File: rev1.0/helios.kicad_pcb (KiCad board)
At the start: 4 copper layers, 17.8 x 33 mm, 61 parts, among them J1 USB_C_Receptacle_USB2.0, J2 helios-pinout, Q1 2N7002VC-, Q2 2N7002VC-, SW1 SWITCH, U1 USBLC6-2P6, U2 TLV75533PDQNR, U3 W25Q128JVPIQ, U4 RP2040, U5 74LVC1T45, Y1 12MHz

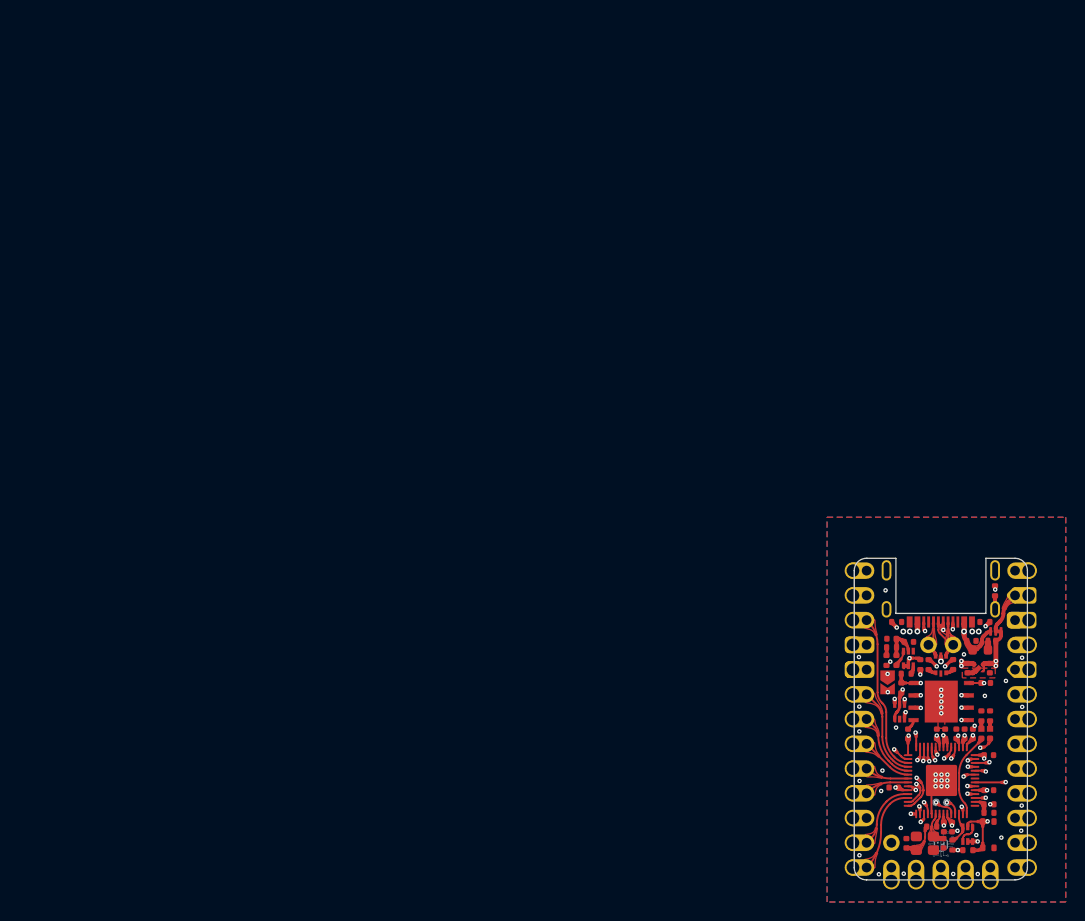
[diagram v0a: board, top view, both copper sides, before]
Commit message: widen tabs
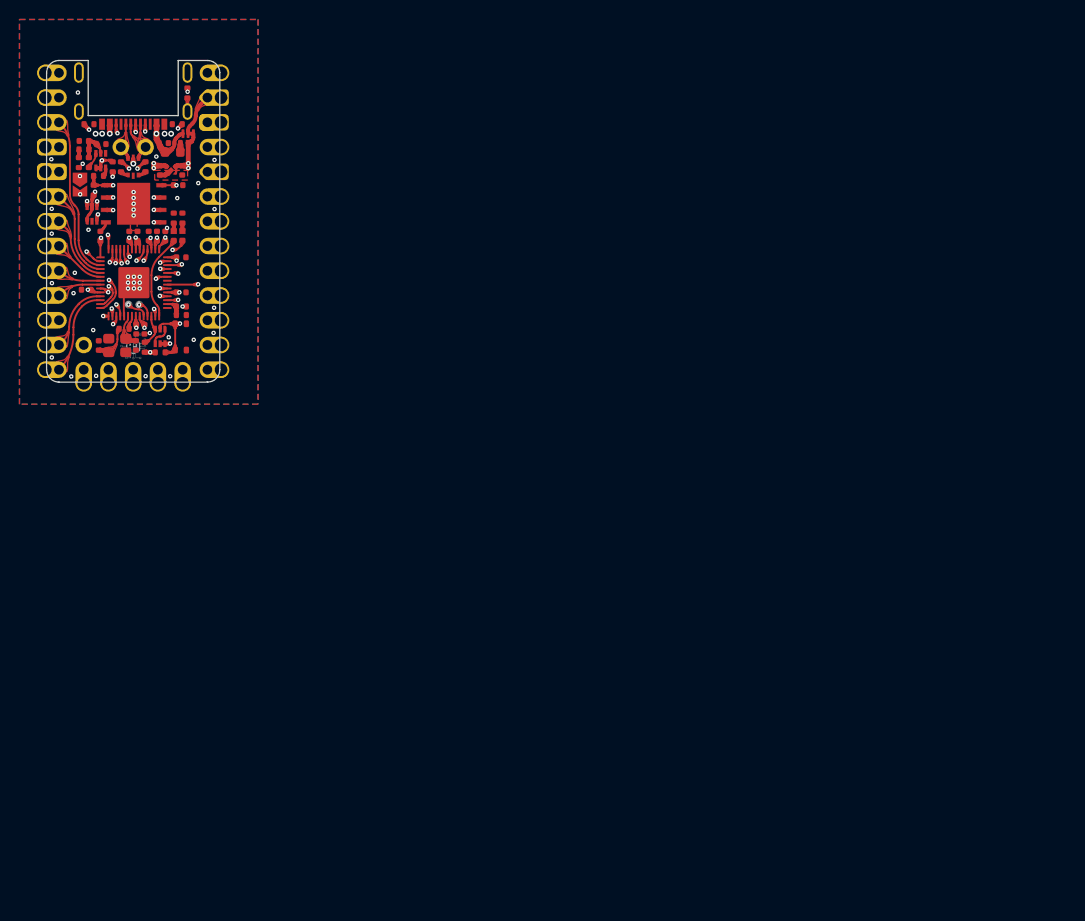
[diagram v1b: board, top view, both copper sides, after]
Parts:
- moved REF** 97.7 mm to (69.5, 81.2)
- moved R9 97.4 mm to (72.4, 93.6)
- moved SW1 97.4 mm to (80.8, 110.2)
- moved U1 97.4 mm to (75.9, 92.7)
- moved C1 97.4 mm to (70.9, 90.0)
- moved C12 97.4 mm to (80.9, 105.6)
- moved C14 97.4 mm to (76.4, 99.8)
- moved C15 97.4 mm to (71.1, 105.3)
- moved C16 97.4 mm to (72.6, 99.8)
- moved C3 97.4 mm to (79.1, 90.3)
- moved C9 97.4 mm to (78.4, 99.8)
- moved D2 97.4 mm to (80.1, 99.8)
- moved JP2 97.4 mm to (81.6, 89.3)
- moved Q2 97.4 mm to (72.6, 92.1)
- moved R1 97.4 mm to (78.7, 111.8)
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
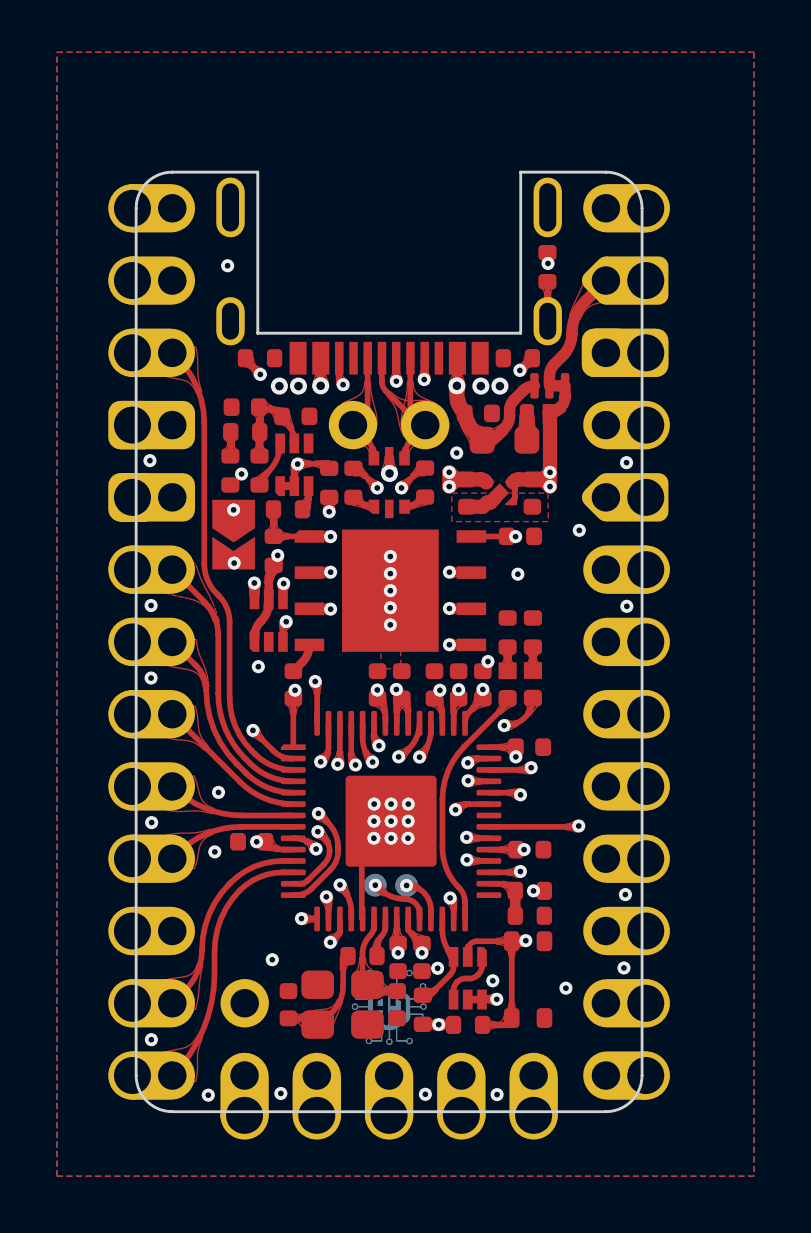
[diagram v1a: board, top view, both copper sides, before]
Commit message: widen tabs even more
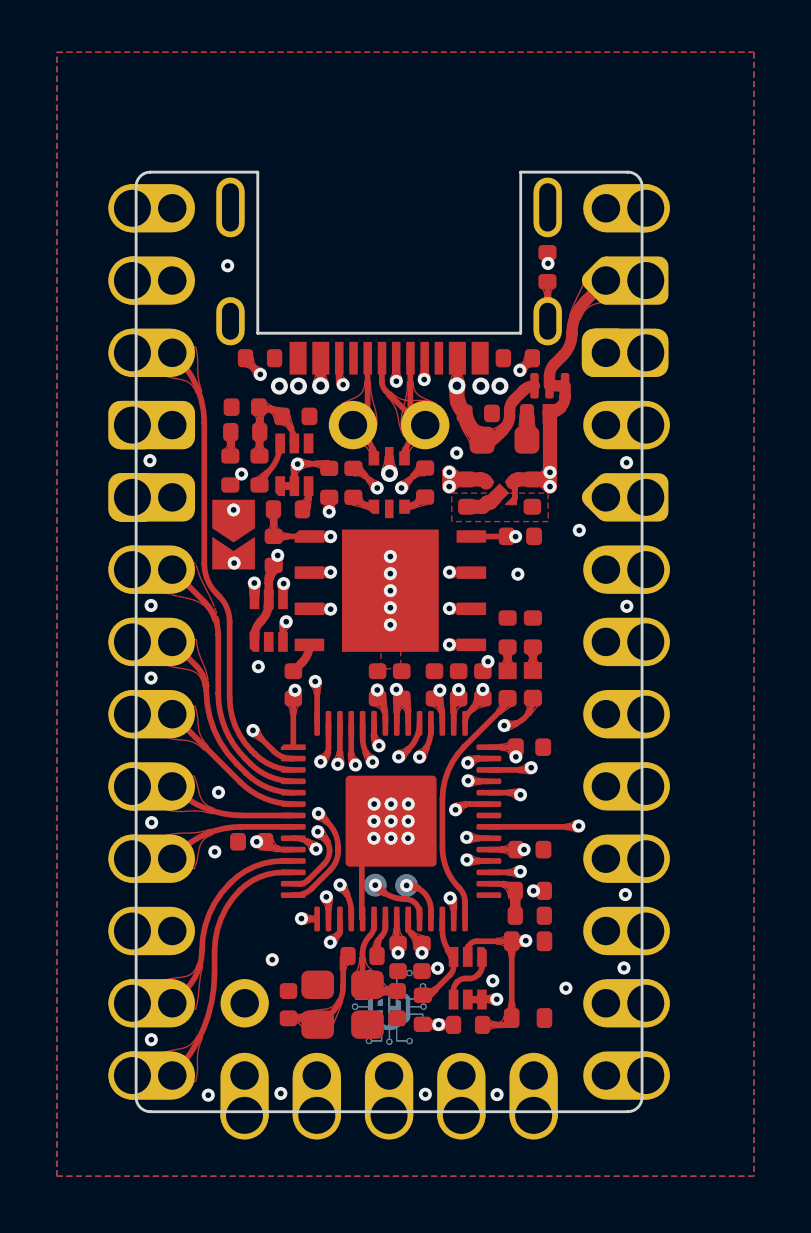
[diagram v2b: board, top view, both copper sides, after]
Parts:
- removed the REF** at (82.8, 115.2)
- removed the REF** at (69.1, 115.2)
- added REF**: Tab, kikit:Tab, F.Cu at (83.3, 115.3)
- added REF**: Tab, kikit:Tab, F.Cu at (68.6, 115.3)
- moved REF** 0.30 mm to (82.6, 81.3)
- moved REF** 0.28 mm to (69.3, 81.3)
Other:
- outline, holes or cut-outs redrawn
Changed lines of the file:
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@@
         (effects (font (size 0.8 0.8) (thickness 0.12)) (justify mirror))
     )
-    (fp_line (start -8.89 -16.51) (end -8.89 13.97)
+    (fp_line (start -8.89 -17.28) (end -8.89 14.74)
       (stroke (width 0.1) (type solid)) (layer "Edge.Cuts"))
-    (fp_line (start -7.62 15.24) (end 7.62 15.24)
+    (fp_line (start -8.39 15.24) (end 8.39 15.24)
       (stroke (width 0.1) (type solid)) (layer "Edge.Cuts"))
-    (fp_line (start 8.89 13.97) (end 8.89 -16.51)
-      (stroke (width 0.1) (type solid)) (layer "Edge.Cuts"))
-    (fp_arc (start -8.89 -16.51) (mid -8.518026 -17.408026) (end -7.62 -17.78)
-      (stroke (width 0.1) (type solid)) (layer "Edge.Cuts"))
-    (fp_arc (start -7.62 15.24) (mid -8.518026 14.868026) (end -8.89 13.97)
-      (stroke (width 0.1) (type solid)) (layer "Edge.Cuts"))
-    (fp_arc (start 7.62 -17.78) (mid 8.518026 -17.408026) (end 8.89 -16.51)
-      (stroke (width 0.1) (type solid)) (layer "Edge.Cuts"))
-    (fp_arc (start 8.89 13.97) (mid 8.518026 14.868026) (end 7.62 15.24)
+    (fp_line (start 8.89 14.74) (end 8.89 -17.28)
       (stroke (width 0.1) (type solid)) (layer "Edge.Cuts"))
+    (fp_arc (start -8.89 -17.28) (mid -8.743553 -17.633553) (end -8.39 -17.78)
+      (stroke (width 0.1) (type default)) (layer "Edge.Cuts"))
+    (fp_arc (start -8.39 15.24) (mid -8.743553 15.093553) (end -8.89 14.74)
+      (stroke (width 0.1) (type default)) (layer "Edge.Cuts"))
+    (fp_arc (start 8.39 -17.78) (mid 8.743553 -17.633553) (end 8.89 -17.28)
+      (stroke (width 0.1) (type default)) (layer "Edge.Cuts"))
+    (fp_arc (start 8.89 14.74) (mid 8.743553 15.093553) (end 8.39 15.24)
+      (stroke (width 0.1) (type default)) (layer "Edge.Cuts"))
     (pad "1" thru_hole circle (at -9.02 -16.51) (size 1.7 1.7) (drill 1.3) (property pad_prop_castellated) (layers "*.Cu" "*.Mask")
       (net 16 "/10") (pinfunction "IO10") (pintype "bidirectional"))
@@
   )
   (footprint "kikit:Tab" (layer "F.Cu")
-    (at 69.53 81.16 -90)
-    (descr "A symbol representing annotation for tab placement")
-    (attr board_only exclude_from_pos_files exclude_from_bom)
-    (fp_text reference "REF**" (at 0 -2 90) (layer "F.SilkS") hide
-        (effects (font (size 1 1) (thickness 0.15)))
-    )
-    (fp_text value "Tab" (at -2.75 -1 90) (layer "Dwgs.User")
-        (effects (font (size 1.2 1.2) (thickness 0.2)))
-    )
-    (fp_text user "KIKIT: width: 3.5mm" (at -5.5 0) (layer "Dwgs.User")
-        (effects (font (size 1 1) (thickness 0.15)))
-    )
-    (fp_line (start 0.25 0) (end -2.75 0)
-      (stroke (width 0.3) (type solid)) (layer "Dwgs.User"))
-    (fp_line (start 0.25 0) (end -0.75 -1)
-      (stroke (width 0.3) (type solid)) (layer "Dwgs.User"))
-    (fp_line (start 0.25 0) (end -0.75 1)
-      (stroke (width 0.3) (type solid)) (layer "Dwgs.User"))
-    (fp_line (start 0.25 1) (end 0.25 -1)
-      (stroke (width 0.3) (type solid)) (layer "Dwgs.User"))
-  )
-  (footprint "kikit:Tab" (layer "F.Cu")
-    (at 82.81 115.25 90)
+    (at 69.31 81.34 -90)
     (descr "A symbol representing annotation for tab placement")
     (attr board_only exclude_from_pos_files exclude_from_bom)
@@
         (effects (font (size 1.2 1.2) (thickness 0.2)))
     )
-    (fp_text user "KIKIT: width: 1.5mm" (at -5.5 0) (layer "Dwgs.User")
+    (fp_text user "KIKIT: width: 4mm" (at -5.5 0) (layer "Dwgs.User")
         (effects (font (size 1 1) (thickness 0.15)))
     )
@@
   )
   (footprint "kikit:Tab" (layer "F.Cu")
-    (at 82.34 81.14 -90)
+    (at 82.57 81.34 -90)
     (descr "A symbol representing annotation for tab placement")
     (attr board_only exclude_from_pos_files exclude_from_bom)
@@
         (effects (font (size 1.2 1.2) (thickness 0.2)))
     )
-    (fp_text user "KIKIT: width: 3.5mm" (at -5.5 0) (layer "Dwgs.User")
+    (fp_text user "KIKIT: width: 4mm" (at -5.5 0) (layer "Dwgs.User")
         (effects (font (size 1 1) (thickness 0.15)))
     )
@@
     )
   )
+  (footprint "kikit:Tab" (layer "F.Cu")
+    (at 83.32 115.27 90)
+    (descr "A symbol representing annotation for tab placement")
+    (attr board_only exclude_from_pos_files exclude_from_bom)
+    (fp_text reference "REF**" (at 0 -2 90) (layer "F.SilkS") hide
+        (effects (font (size 1 1) (thickness 0.15)))
+    )
+    (fp_text value "Tab" (at -2.75 -1 90) (layer "Dwgs.User")
+        (effects (font (size 1.2 1.2) (thickness 0.2)))
+    )
+    (fp_text user "KIKIT: width: 2mm" (at -5.5 0) (layer "Dwgs.User")
+        (effects (font (size 1 1) (thickness 0.15)))
+    )
+    (fp_line (start 0.25 0) (end -2.75 0)
+      (stroke (width 0.3) (type solid)) (layer "Dwgs.User"))
+    (fp_line (start 0.25 0) (end -0.75 -1)
+      (stroke (width 0.3) (type solid)) (layer "Dwgs.User"))
+    (fp_line (start 0.25 0) (end -0.75 1)
+      (stroke (width 0.3) (type solid)) (layer "Dwgs.User"))
+    (fp_line (start 0.25 1) (end 0.25 -1)
+      (stroke (width 0.3) (type solid)) (layer "Dwgs.User"))
+  )
+  (footprint "kikit:Tab" (layer "F.Cu")
+    (at 68.56 115.26 90)
+    (descr "A symbol representing annotation for tab placement")
+    (attr board_only exclude_from_pos_files exclude_from_bom)
+    (fp_text reference "REF**" (at 0 -2 90) (layer "F.SilkS") hide
+        (effects (font (size 1 1) (thickness 0.15)))
+    )
+    (fp_text value "Tab" (at -2.75 -1 90) (layer "Dwgs.User")
+        (effects (font (size 1.2 1.2) (thickness 0.2)))
+    )
+    (fp_text user "KIKIT: width: 2mm" (at -5.5 0) (layer "Dwgs.User")
+        (effects (font (size 1 1) (thickness 0.15)))
+    )
+    (fp_line (start 0.25 0) (end -2.75 0)
+      (stroke (width 0.3) (type solid)) (layer "Dwgs.User"))
+    (fp_line (start 0.25 0) (end -0.75 -1)
+      (stroke (width 0.3) (type solid)) (layer "Dwgs.User"))
+    (fp_line (start 0.25 0) (end -0.75 1)
+      (stroke (width 0.3) (type solid)) (layer "Dwgs.User"))
+    (fp_line (start 0.25 1) (end 0.25 -1)
+      (stroke (width 0.3) (type solid)) (layer "Dwgs.User"))
+  )
   (footprint "0xcb:R_0402_1005Metric" (layer "F.Cu")
     (at 78.71 111.75)
@@
     )
   )
-  (footprint "kikit:Tab" (layer "F.Cu")
-    (at 69.06 115.25 90)
-    (descr "A symbol representing annotation for tab placement")
-    (attr board_only exclude_from_pos_files exclude_from_bom)
-    (fp_text reference "REF**" (at 0 -2 90) (layer "F.SilkS") hide
-        (effects (font (size 1 1) (thickness 0.15)))
-    )
-    (fp_text value "Tab" (at -2.75 -1 90) (layer "Dwgs.User")
-        (effects (font (size 1.2 1.2) (thickness 0.2)))
-    )
-    (fp_text user "KIKIT: width: 1.5mm" (at -5.5 0) (layer "Dwgs.User")
-        (effects (font (size 1 1) (thickness 0.15)))
-    )
-    (fp_line (start 0.25 0) (end -2.75 0)
-      (stroke (width 0.3) (type solid)) (layer "Dwgs.User"))
-    (fp_line (start 0.25 0) (end -0.75 -1)
-      (stroke (width 0.3) (type solid)) (layer "Dwgs.User"))
-    (fp_line (start 0.25 0) (end -0.75 1)
-      (stroke (width 0.3) (type solid)) (layer "Dwgs.User"))
-    (fp_line (start 0.25 1) (end 0.25 -1)
-      (stroke (width 0.3) (type solid)) (layer "Dwgs.User"))
-  )
   (footprint "0xcb:C_0402_1005Metric" (layer "F.Cu")
     (at 80.97 93.06 -90)
@@
       (net 54 "/SWD_IO") (pinfunction "1") (pintype "passive"))
   )
-  (gr_line (start 71.32 81.78) (end 68.315 81.78)
+  (gr_line (start 71.32 81.78) (end 67.545 81.78)
     (stroke (width 0.1) (type solid)) (layer "Edge.Cuts"))
   (gr_line (start 71.32 81.78) (end 71.32 87.44)
@@
   (gr_line (start 80.56 87.44) (end 80.56 81.78)
     (stroke (width 0.1) (type solid)) (layer "Edge.Cuts"))
-  (gr_line (start 80.56 81.78) (end 83.555 81.78)
+  (gr_line (start 80.56 81.78) (end 84.325 81.78)
     (stroke (width 0.1) (type solid)) (layer "Edge.Cuts"))
   (segment (start 71.38 91.755) (end 71.38 90.925) (width 0.2) (layer "F.Cu") (net 1))

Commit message: manu change
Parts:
- removed the REF** at (69.3, 81.3)
- removed the REF** at (82.6, 81.3)
- removed the REF** at (83.3, 115.3)
- removed the REF** at (68.6, 115.3)
- C1: value 4u7 -> 4.7u
- R12, R13: value 27R -> 27
- R16, R7, R8: value 5k1 -> 5.1k
- R4, R5, R6: value 51K -> 51k
- R9: value 1K -> 1k
- moved R10 2.69 mm to (83.5, 99.0)
- moved R15 2.69 mm to (82.6, 99.0)
- moved R7 2.69 mm to (82.9, 89.4)
- moved TP2 2.69 mm to (79.0, 107.9)
- moved C1 2.69 mm to (73.3, 91.1)
- moved C12 2.69 mm to (83.3, 106.7)
- moved C14 2.69 mm to (78.8, 100.9)
- moved C16 2.69 mm to (75.0, 100.9)
- moved C3 2.69 mm to (81.5, 91.3)
- moved C4 2.69 mm to (83.4, 94.1)
- moved C6 2.69 mm to (83.0, 95.7)
- moved C7 2.69 mm to (78.7, 112.1)
- moved C9 2.69 mm to (80.8, 100.9)
- moved D1 2.69 mm to (83.5, 100.9)
- moved D2 2.69 mm to (82.6, 100.9)
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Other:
- board size 17.8 x 33 mm -> 16.4 x 43.4 mm
